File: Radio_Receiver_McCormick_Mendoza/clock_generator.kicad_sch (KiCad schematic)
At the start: 0 parts

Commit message: slight updates to the KiCad files
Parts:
- added Y1: Si5351A-B-GM, Package_DFN_QFN:QFN-20-1EP_4x4mm_P0.5mm_EP2.7x2.7mm, symbol Oscillator:Si5351A-B-GM
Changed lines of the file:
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@@
 		(comment 3 "Jeffrey McCormick")
 	)
+	(symbol
+		(lib_id "Oscillator:Si5351A-B-GM")
+		(at 101.6 73.66 0)
+		(unit 1)
+		(body_style 1)
+		(exclude_from_sim no)
+		(in_bom yes)
+		(on_board yes)
+		(in_pos_files yes)
+		(dnp no)
+		(fields_autoplaced yes)
+		(property "Reference" "Y1"
+			(at 103.7433 96.52 0)
+			(show_name no)
+			(do_not_autoplace no)
+			(effects
+				(font
+					(size 1.27 1.27)
+				)
+				(justify left)
+			)
+		)
+		(property "Value" "Si5351A-B-GM"
+			(at 103.7433 99.06 0)
+			(show_name no)
+			(do_not_autoplace no)
+			(effects
+				(font
+					(size 1.27 1.27)
+				)
+				(justify left)
+			)
+		)
+		(property "Footprint" "Package_DFN_QFN:QFN-20-1EP_4x4mm_P0.5mm_EP2.7x2.7mm"
+			(at 101.6 104.14 0)
+			(hide yes)
+			(show_name no)
+			(do_not_autoplace no)
+			(effects
+				(font
+					(size 1.27 1.27)
+				)
+			)
+		)
+		(property "Datasheet" "https://www.silabs.com/documents/public/data-sheets/Si5351-B.pdf"
+			(at 101.6 73.66 0)
+			(hide yes)
+			(show_name no)
+			(do_not_autoplace no)
+			(effects
+				(font
+					(size 1.27 1.27)
+				)
+			)
+		)
+		(property "Description" "I2C Programmable Any-Frequency CMOS Clock Generator, QFN-20"
+			(at 101.6 73.66 0)
+			(hide yes)
+			(show_name no)
+			(do_not_autoplace no)
+			(effects
+				(font
+					(size 1.27 1.27)
+				)
+			)
+		)
+		(pin "13"
+		)
+		(pin "17"
+		)
+		(pin "19"
+		)
+		(pin "6"
+		)
+		(pin "8"
+		)
+		(pin "9"
+		)
+		(pin "11"
+		)
+		(pin "12"
+		)
+		(pin "14"
+		)
+		(pin "3"
+		)
+		(pin "7"
+		)
+		(pin "15"
+		)
+		(pin "1"
+		)
+		(pin "2"
+		)
+		(pin "5"
+		)
+		(pin "4"
+		)
+		(pin "10"
+		)
+		(pin "16"
+		)
+		(pin "18"
+		)
+		(pin "21"
+		)
+		(pin "20"
+		)
+		(instances
+			(project "Radio_Receiver_McCormick_Mendoza"
+				(path "/f31d31ab-6846-4f3a-92b1-aa5a6a13373f/f64ea8ac-f7b3-4ac7-b675-bede152c9b4e"
+					(reference "Y1")
+					(unit 1)
+				)
+			)
+		)
+	)
 )

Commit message: Merge conflict resolution.
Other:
- title: (none) -> Radio Receiver
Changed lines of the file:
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@@
 	(paper "A4")
 	(title_block
+		(title "Radio Receiver")
 		(date "2026-04-19")
 		(rev "0.0.1")

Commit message: Propogated Title Block Fields
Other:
- company: (none) -> Walla Walla University
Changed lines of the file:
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@@
 		(date "2026-04-19")
 		(rev "0.0.1")
+		(company "Walla Walla University")
 		(comment 2 "Daniel Mendoza")
 		(comment 3 "Jeffrey McCormick")

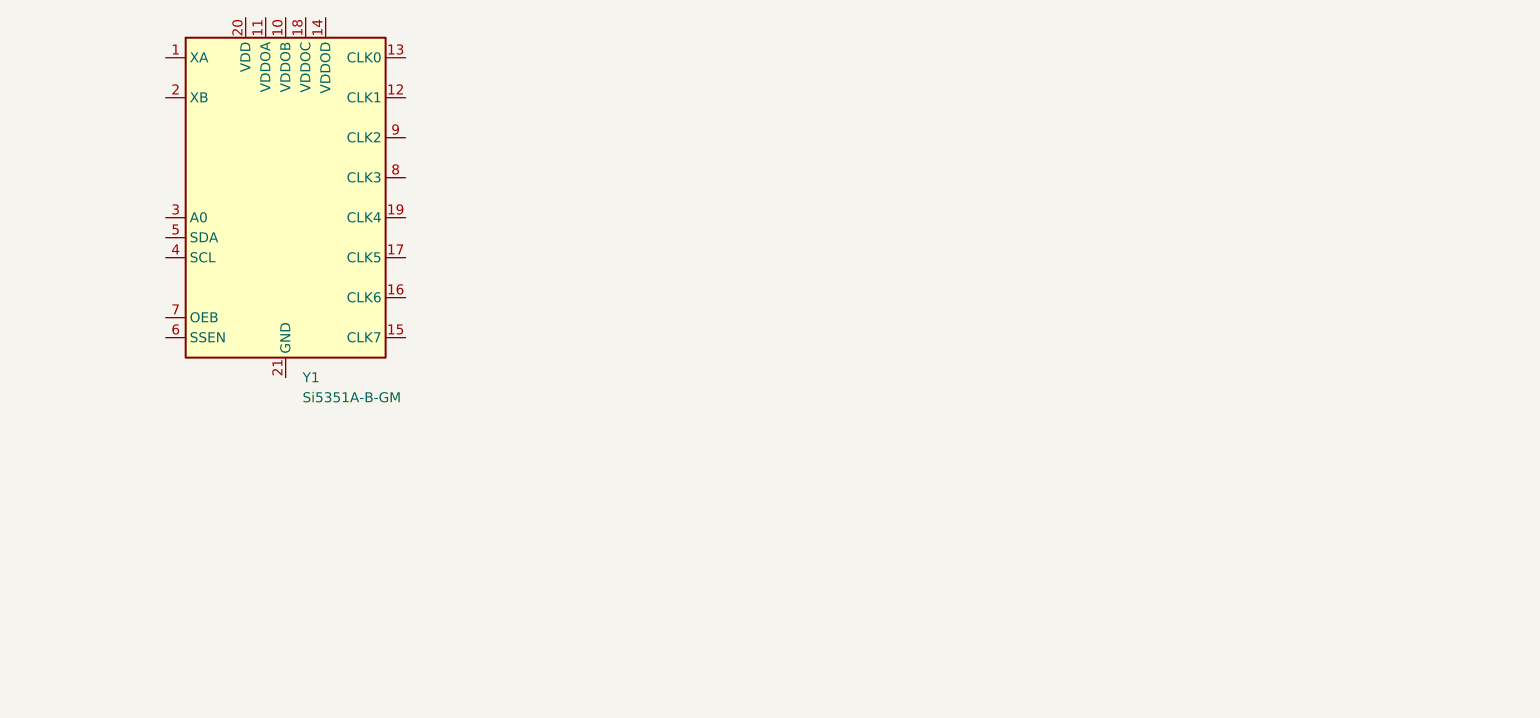
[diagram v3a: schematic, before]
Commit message: Added Daniel Mendoza's changes to KiCAD files.
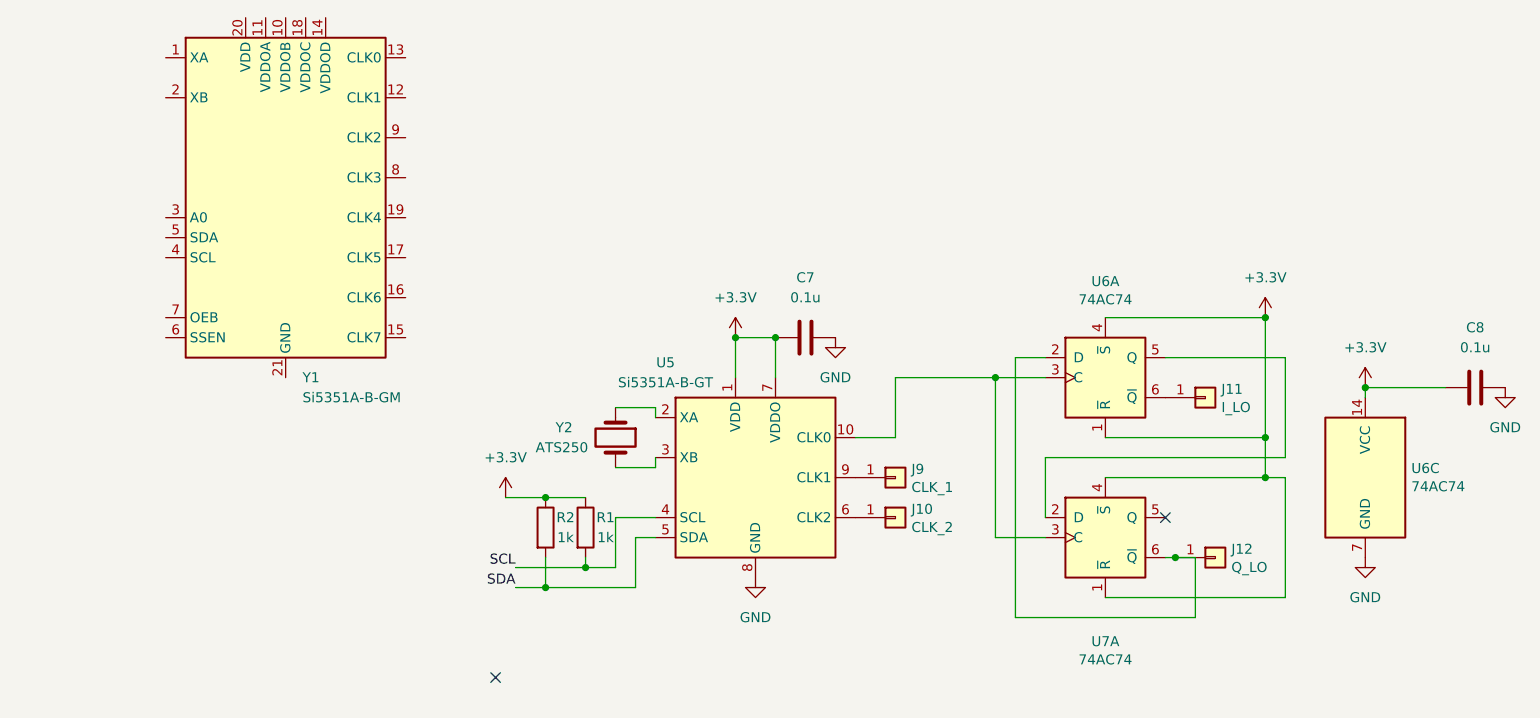
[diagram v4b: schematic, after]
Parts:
- added C7, C8: 0.1u, Capacitor_THT:C_Disc_D5.1mm_W3.2mm_P5.00mm, symbol Device:C
- added J10: CLK_2, Connector_PinHeader_2.54mm:PinHeader_1x01_P2.54mm_Vertical, symbol Connector_Generic:Conn_01x01
- added J11: I_LO, Connector_PinHeader_2.54mm:PinHeader_1x01_P2.54mm_Vertical, symbol Connector_Generic:Conn_01x01
- added J12: Q_LO, Connector_PinHeader_2.54mm:PinHeader_1x01_P2.54mm_Vertical, symbol Connector_Generic:Conn_01x01
- added J9: CLK_1, Connector_PinHeader_2.54mm:PinHeader_1x01_P2.54mm_Vertical, symbol Connector_Generic:Conn_01x01
- added R1, R2: 1k, symbol Device:R
- added U5: Si5351A-B-GT, Package_SO:MSOP-10_3x3mm_P0.5mm, symbol Oscillator:Si5351A-B-GT
- added U6, U7: 74AC74, Package_DIP:DIP-14_W7.62mm, symbol 74xx:74HC74
- added Y2: ATS250, Crystal:Crystal_HC49-U_Vertical, symbol Device:Crystal
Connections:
- new net: J9.1 (Pin_1), U5.9 (CLK1)
- new net: J12.1 (Pin_1), U6.2 (D), U7.6 (~{Q})
- new net: U5.10 (CLK0), U6.3 (C), U7.3 (C)
- new net: U6.5 (Q), U7.2 (D)
- new net: J11.1 (Pin_1), U6.6 (~{Q})
- new net: U5.2 (XA), Y2.1
- new net: U5.3 (XB), Y2.2
- new net: J10.1 (Pin_1), U5.6 (CLK2)
- new net +3.3V: C7.1, C8.1, R1.1, R2.1, U5.1 (VDD), U5.7 (VDDO), U6.1 (~{R}), U6.14 (VCC), U6.4 (~{S}), U7.1 (~{R}), U7.4 (~{S})
- new net GND: C7.2, C8.2, U5.8 (GND), U6.7 (GND)
- new net SCL: R1.2, U5.4 (SCL)
- new net SDA: R2.2, U5.5 (SDA)
- no-connect marks 0 -> 2

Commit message: Added footprints
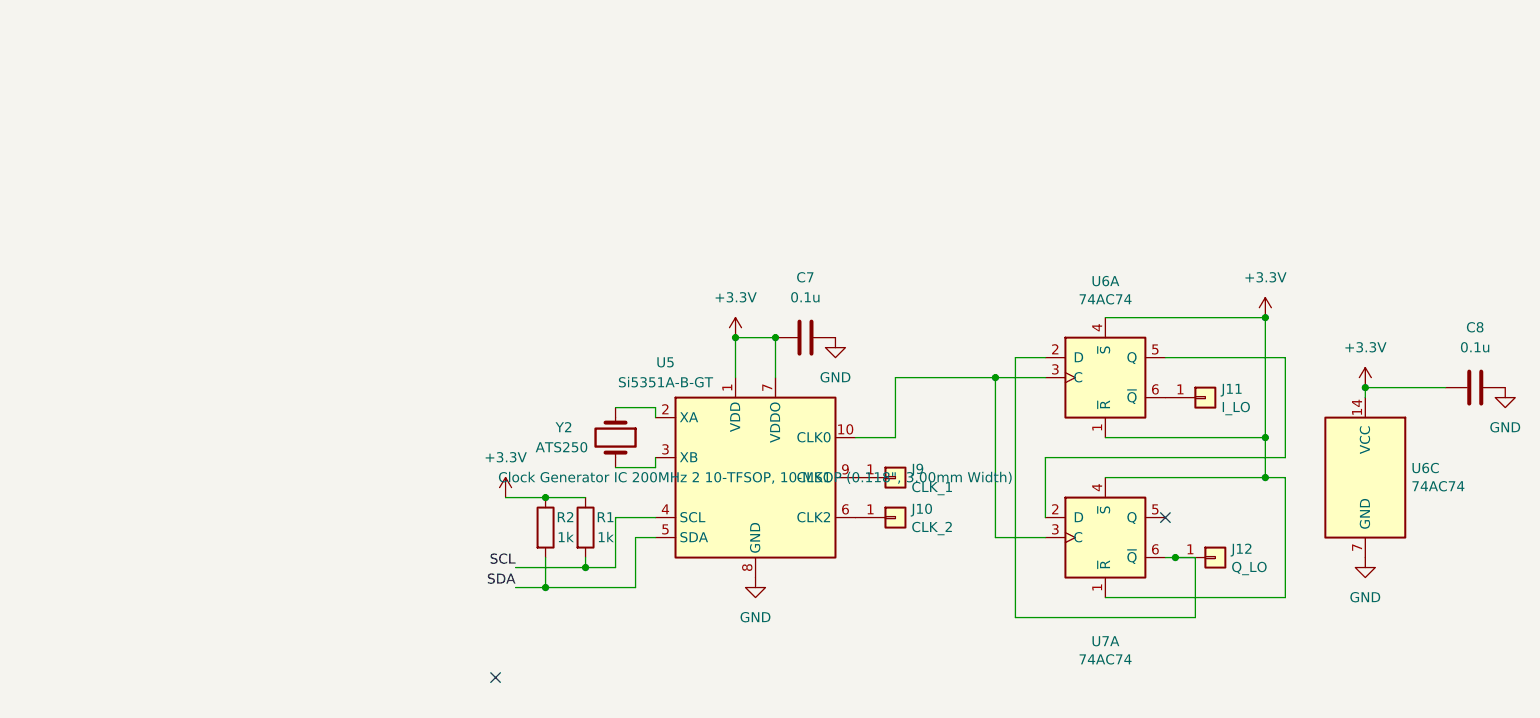
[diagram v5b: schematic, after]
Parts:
- removed Y1: Si5351A-B-GM, Package_DFN_QFN:QFN-20-1EP_4x4mm_P0.5mm_EP2.7x2.7mm, symbol Oscillator:Si5351A-B-GM
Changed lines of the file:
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@@
-	)
-	(symbol
-		(lib_id "Oscillator:Si5351A-B-GM")
-		(at 101.6 73.66 0)
-		(unit 1)
-		(body_style 1)
-		(exclude_from_sim no)
-		(in_bom yes)
-		(on_board yes)
-		(in_pos_files yes)
-		(dnp no)
-		(fields_autoplaced yes)
-		(property "Reference" "Y1"
-			(at 103.7433 96.52 0)
-			(show_name no)
-			(do_not_autoplace no)
-			(effects
-				(font
-					(size 1.27 1.27)
-				)
-				(justify left)
-			)
-		)
-		(property "Value" "Si5351A-B-GM"
-			(at 103.7433 99.06 0)
-			(show_name no)
-			(do_not_autoplace no)
-			(effects
-				(font
-					(size 1.27 1.27)
-				)
-				(justify left)
-			)
-		)
-		(property "Footprint" "Package_DFN_QFN:QFN-20-1EP_4x4mm_P0.5mm_EP2.7x2.7mm"
-			(at 101.6 104.14 0)
-			(hide yes)
-			(show_name no)
-			(do_not_autoplace no)
-			(effects
-				(font
-					(size 1.27 1.27)
-				)
-			)
-		)
-		(property "Datasheet" "https://www.silabs.com/documents/public/data-sheets/Si5351-B.pdf"
-			(at 101.6 73.66 0)
-			(hide yes)
-			(show_name no)
-			(do_not_autoplace no)
-			(effects
-				(font
-					(size 1.27 1.27)
-				)
-			)
-		)
-		(property "Description" "I2C Programmable Any-Frequency CMOS Clock Generator, QFN-20"
-			(at 101.6 73.66 0)
-			(hide yes)
-			(show_name no)
-			(do_not_autoplace no)
-			(effects
-				(font
-					(size 1.27 1.27)
-				)
-			)
-		)
-		(pin "13"
-		)
-		(pin "17"
-		)
-		(pin "19"
-		)
-		(pin "6"
-		)
-		(pin "8"
-		)
-		(pin "9"
-		)
-		(pin "11"
-		)
-		(pin "12"
-		)
-		(pin "14"
-		)
-		(pin "3"
-		)
-		(pin "7"
-		)
-		(pin "15"
-		)
-		(pin "1"
-		)
-		(pin "2"
-		)
-		(pin "5"
-		)
-		(pin "4"
-		)
-		(pin "10"
-		)
-		(pin "16"
-		)
-		(pin "18"
-		)
-		(pin "21"
-		)
-		(pin "20"
-		)
-		(instances
-			(project "Radio_Receiver_McCormick_Mendoza"
-				(path "/f31d31ab-6846-4f3a-92b1-aa5a6a13373f/f64ea8ac-f7b3-4ac7-b675-bede152c9b4e"
-					(reference "Y1")
-					(unit 1)
-				)
-			)
-		)
 	)
 	(symbol
@@
 			)
 		)
-		(property "Datasheet" "https://www.silabs.com/documents/public/data-sheets/Si5351-B.pdf"
+		(property "Datasheet" "https://www.skyworksinc.com/-/media/Skyworks/SL/documents/public/data-sheets/Si5351-B.pdf"
 			(at 152.4 111.76 0)
 			(hide yes)
@@
 			)
 		)
-		(property "Description" ""
+		(property "Description" "Clock Generator IC 200MHz 2 10-TFSOP, 10-MSOP (0.118\", 3.00mm Width)"
 			(at 161.29 109.22 0)
 			(show_name no)

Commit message: Schematic connection edits
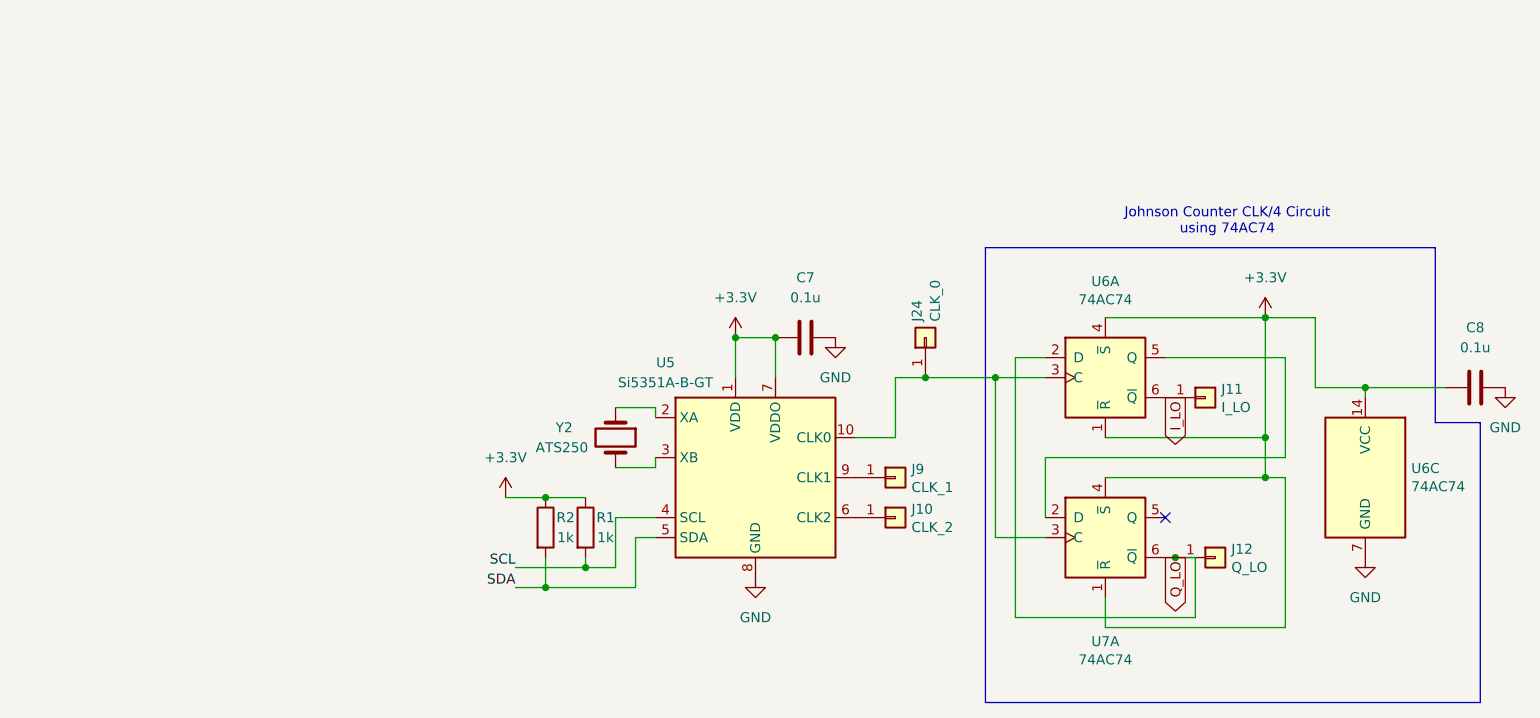
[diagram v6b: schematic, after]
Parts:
- added J24: CLK_0, Connector_PinHeader_2.54mm:PinHeader_1x01_P2.54mm_Vertical, symbol Connector_Generic:Conn_01x01
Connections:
- net Q_LO: now reaches J12.1 (Pin_1), U6.2 (D), U7.6 (~{Q})
- net at U5.10 (CLK0), U6.3 (C), U7.3 (C): now also J24.1 (Pin_1)
- no-connect marks 2 -> 1
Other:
- note added: "Johnson Counter CLK/4 Circuit using 74AC74"
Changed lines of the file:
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@@
 		(comment 3 "Jeffrey McCormick")
+	)
+	(text "Johnson Counter CLK/4 Circuit\nusing 74AC74"
+		(exclude_from_sim no)
+		(at 221.234 76.708 0)
+		(effects
+			(font
+				(size 1.27 1.27)
+			)
+		)
 	)
 	(junction
@@
 	)
 	(junction
+		(at 182.88 96.52)
+		(diameter 0)
+		(color 0 0 0 0)
+	)
+	(junction
 		(at 139.7 120.65)
 		(diameter 0)
@@
 		(at 213.36 114.3)
 	)
-	(no_connect
-		(at 128.27 134.62)
-	)
 	(wire
 		(pts
@@
 	(wire
 		(pts
-			(xy 205.74 124.46) (xy 228.6 124.46)
+			(xy 182.88 96.52) (xy 191.77 96.52)
+		)
+		(stroke
+			(width 0)
+			(type default)
+		)
+	)
+	(wire
+		(pts
+			(xy 205.74 128.27) (xy 228.6 128.27)
+		)
+		(stroke
+			(width 0)
+			(type default)
+		)
+	)
+	(wire
+		(pts
+			(xy 238.76 97.79) (xy 232.41 97.79)
 		)
 		(stroke
@@
 		)
 	)
+	(polyline
+		(pts
+			(xy 190.5 80.01) (xy 190.5 137.795)
+		)
+		(stroke
+			(width 0)
+			(type default)
+		)
+	)
 	(wire
 		(pts
@@
 	(wire
 		(pts
-			(xy 228.6 109.22) (xy 228.6 124.46)
+			(xy 228.6 109.22) (xy 228.6 128.27)
 		)
 		(stroke
@@
 	(wire
 		(pts
+			(xy 205.74 128.27) (xy 205.74 124.46)
+		)
+		(stroke
+			(width 0)
+			(type default)
+		)
+	)
+	(wire
+		(pts
 			(xy 228.6 93.98) (xy 213.36 93.98)
 		)
@@
 	(wire
 		(pts
+			(xy 232.41 88.9) (xy 226.06 88.9)
+		)
+		(stroke
+			(width 0)
+			(type default)
+		)
+	)
+	(polyline
+		(pts
+			(xy 253.365 102.235) (xy 247.65 102.235)
+		)
+		(stroke
+			(width 0)
+			(type default)
+		)
+	)
+	(wire
+		(pts
 			(xy 158.75 91.44) (xy 158.75 96.52)
 		)
@@
 		)
 	)
+	(polyline
+		(pts
+			(xy 253.365 137.795) (xy 253.365 102.235)
+		)
+		(stroke
+			(width 0)
+			(type default)
+		)
+	)
+	(polyline
+		(pts
+			(xy 190.5 80.01) (xy 247.65 80.01)
+		)
+		(stroke
+			(width 0)
+			(type default)
+		)
+	)
 	(wire
 		(pts
@@
 		)
 	)
+	(polyline
+		(pts
+			(xy 247.65 102.235) (xy 247.65 80.01)
+		)
+		(stroke
+			(width 0)
+			(type default)
+		)
+	)
+	(wire
+		(pts
+			(xy 232.41 97.79) (xy 232.41 88.9)
+		)
+		(stroke
+			(width 0)
+			(type default)
+		)
+	)
 	(wire
 		(pts
@@
 	(wire
 		(pts
-			(xy 179.07 96.52) (xy 191.77 96.52)
+			(xy 179.07 96.52) (xy 182.88 96.52)
 		)
 		(stroke
@@
 		(pts
 			(xy 226.06 88.9) (xy 226.06 104.14)
+		)
+		(stroke
+			(width 0)
+			(type default)
+		)
+	)
+	(polyline
+		(pts
+			(xy 190.5 137.795) (xy 253.365 137.795)
 		)
 		(stroke
@@
 			)
 			(justify right bottom)
+		)
+	)
+	(global_label "Q_LO"
+		(shape output)
+		(at 214.63 119.38 270)
+		(fields_autoplaced yes)
+		(effects
+			(font
+				(size 1.27 1.27)
+			)
+			(justify right)
+		)
+		(property "Intersheetrefs" "${INTERSHEET_REFS}"
+			(at 214.63 127.0219 90)
+			(hide yes)
+			(show_name no)
+			(do_not_autoplace no)
+			(effects
+				(font
+					(size 1.27 1.27)
+				)
+				(justify right)
+			)
+		)
+	)
+	(global_label "I_LO"
+		(shape output)
+		(at 214.63 99.06 270)
+		(fields_autoplaced yes)
+		(effects
+			(font
+				(size 1.27 1.27)
+			)
+			(justify right)
+		)
+		(property "Intersheetrefs" "${INTERSHEET_REFS}"
+			(at 214.63 105.9762 90)
+			(hide yes)
+			(show_name no)
+			(do_not_autoplace no)
+			(effects
+				(font
+					(size 1.27 1.27)
+				)
+				(justify right)
+			)
 		)
 	)
@@
 	)
 	(symbol
+		(lib_id "Connector_Generic:Conn_01x01")
+		(at 182.88 91.44 90)
+		(unit 1)
+		(body_style 1)
+		(exclude_from_sim no)
+		(in_bom yes)
+		(on_board yes)
+		(in_pos_files yes)
+		(dnp no)
+		(property "Reference" "J24"
+			(at 181.8132 89.408 0)
+			(show_name no)
+			(do_not_autoplace no)
+			(effects
+				(font
+					(size 1.27 1.27)
+				)
+				(justify left)
+			)
+		)
+		(property "Value" "CLK_0"
+			(at 184.1246 89.408 0)
+			(show_name no)
+			(do_not_autoplace no)
+			(effects
+				(font
+					(size 1.27 1.27)
+				)
+				(justify left)
+			)
+		)
+		(property "Footprint" "Connector_PinHeader_2.54mm:PinHeader_1x01_P2.54mm_Vertical"
+			(at 182.88 91.44 0)
+			(hide yes)
+			(show_name no)
+			(do_not_autoplace no)
+			(effects
+				(font
+					(size 1.27 1.27)
+				)
+			)
+		)
+		(property "Datasheet" "~"
+			(at 182.88 91.44 0)
+			(hide yes)
+			(show_name no)
+			(do_not_autoplace no)
+			(effects
+				(font
+					(size 1.27 1.27)
+				)
+			)
+		)
+		(property "Description" ""
+			(at 182.88 91.44 0)
+			(show_name no)
+			(do_not_autoplace no)
+			(effects
+				(font
+					(size 1.27 1.27)
+				)
+			)
+		)
+		(pin "1"
+		)
+		(instances
+			(project "Radio_Receiver_McCormick_Mendoza"
+				(path "/f31d31ab-6846-4f3a-92b1-aa5a6a13373f/f64ea8ac-f7b3-4ac7-b675-bede152c9b4e"
+					(reference "J24")
+					(unit 1)
+				)
+			)
+		)
+	)
+	(symbol
 		(lib_id "Device:C")
 		(at 252.73 97.79 90)
@@
 		)
 		(property "Description" "Clock Generator IC 200MHz 2 10-TFSOP, 10-MSOP (0.118\", 3.00mm Width)"
-			(at 161.29 109.22 0)
+			(at 161.544 133.604 0)
+			(hide yes)
 			(show_name no)
 			(do_not_autoplace no)
@@
 					(unit 1)
 				)
-			)
-		)
-	)
-	(symbol
-		(lib_id "power:+3.3V")
-		(at 238.76 97.79 0)
-		(unit 1)
-		(body_style 1)
-		(exclude_from_sim no)
-		(in_bom yes)
-		(on_board yes)
-		(in_pos_files yes)
-		(dnp no)
-		(fields_autoplaced yes)
-		(property "Reference" "#PWR037"
-			(at 238.76 101.6 0)
-			(hide yes)
-			(show_name no)
-			(do_not_autoplace no)
-			(effects
-				(font
-					(size 1.27 1.27)
-				)
-			)
-		)
-		(property "Value" "+3.3V"
-			(at 238.76 92.71 0)
-			(show_name no)
-			(do_not_autoplace no)
-			(effects
-				(font
-					(size 1.27 1.27)
-				)
-			)
-		)
-		(property "Footprint" ""
-			(at 238.76 97.79 0)
-			(hide yes)
-			(show_name no)
-			(do_not_autoplace no)
-			(effects
-				(font
-					(size 1.27 1.27)
-				)
-			)
-		)
-		(property "Datasheet" ""
-			(at 238.76 97.79 0)
-			(hide yes)
-			(show_name no)
-			(do_not_autoplace no)
-			(effects
-				(font
-					(size 1.27 1.27)
-				)
-			)
-		)
-		(property "Description" "Power symbol creates a global label with name \"+3.3V\""
-			(at 238.76 97.79 0)
-			(hide yes)
-			(show_name no)
-			(do_not_autoplace no)
-			(effects
-				(font
-					(size 1.27 1.27)
-				)
-			)
-		)
-		(pin "1"
-		)
-		(instances
-			(project "Radio_Receiver_McCormick_Mendoza"
-				(path "/f31d31ab-6846-4f3a-92b1-aa5a6a13373f/f64ea8ac-f7b3-4ac7-b675-bede152c9b4e"
-					(reference "#PWR037")
-					(unit 1)
-				)

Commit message: Schematic edits power and signal systems
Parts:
- Y2: value ATS250 -> ASTX-H11-24.576MHZ-T; footprint Crystal:Crystal_HC49-U_Vertical -> (none)
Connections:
- net I_LO: now also J11.1 (Pin_1), U6.6 (~{Q})
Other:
- moved on the sheet: J11, J12, R1, R2, Y2
